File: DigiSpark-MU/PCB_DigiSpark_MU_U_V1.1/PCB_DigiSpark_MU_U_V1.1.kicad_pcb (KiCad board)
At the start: 2 copper layers, 17 x 12 mm, 14 parts, among them J1 USB_A, J2 Conn_01x04, SW1 SW_Push

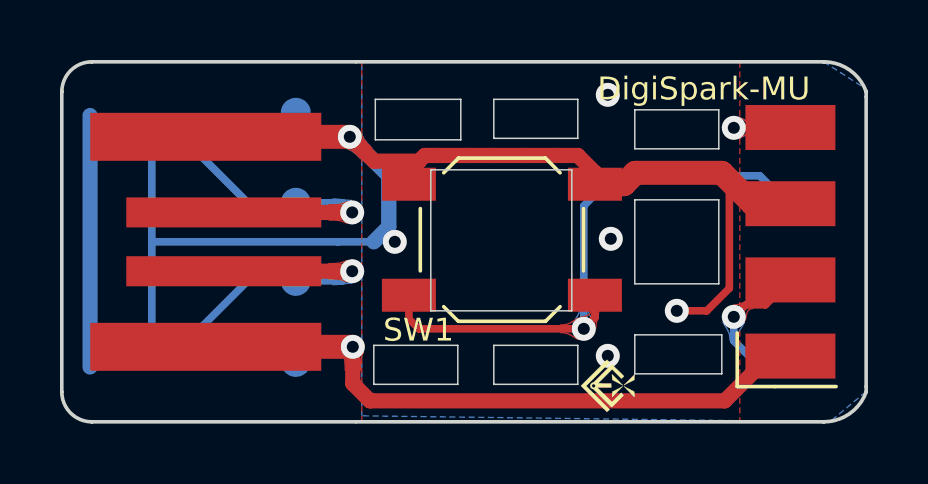
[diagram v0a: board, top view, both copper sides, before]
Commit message: fix silks
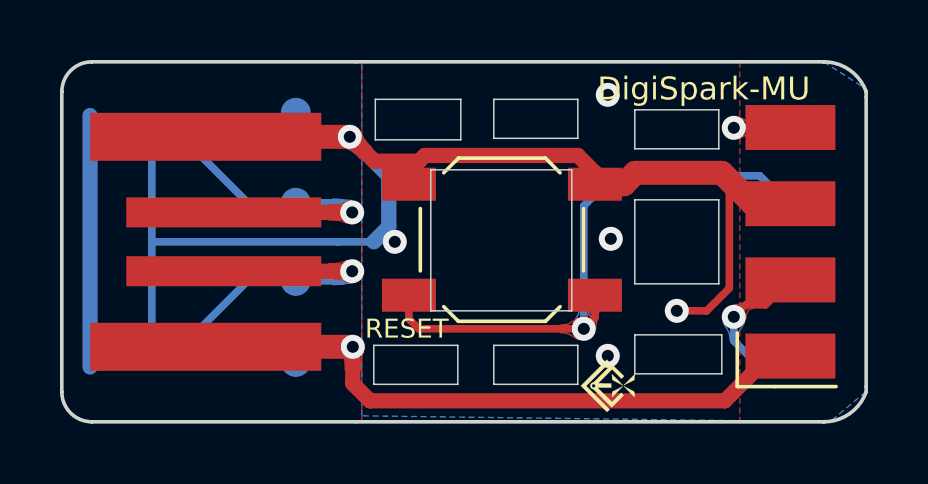
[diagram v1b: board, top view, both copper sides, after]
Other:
- board text added: "RESET"
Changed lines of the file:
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@@
   (general
     (thickness 1)
-    (drawings 40)
+    (drawings 41)
     (tracks 88)
     (zones 0)
@@
   (title_block
     (title PCB_DigiSpark_MU_U)
+    (rev V1.2)
     (company LEXSION.COM)
   )
@@
     (tags "SPST Button Switch")
     (attr smd)
-    (fp_text reference SW1 (at 2.7813 -3.0099) (layer F.SilkS)
+    (fp_text reference SW1 (at 2.7813 -3.0099) (layer F.SilkS) hide
       (effects (font (size 0.762 0.762) (thickness 0.127)))
     )
@@
     (tags "test point SMD pad")
     (attr virtual)
-    (fp_text reference TP6 (at 0.3894 1.107866) (layer B.SilkS)
+    (fp_text reference TP6 (at 0.3 1.333334) (layer B.SilkS)
       (effects (font (size 1 1) (thickness 0.15)) (justify mirror))
     )
@@
     (tags "test point SMD pad")
     (attr virtual)
-    (fp_text reference TP5 (at 0.364 1.114533) (layer B.SilkS)
+    (fp_text reference TP5 (at 0.3 1.366667) (layer B.SilkS)
       (effects (font (size 1 1) (thickness 0.15)) (justify mirror))
     )
@@
     (tags "test point SMD pad")
     (attr virtual)
-    (fp_text reference TP4 (at 0.364 1.1466) (layer B.SilkS)
+    (fp_text reference TP4 (at 0.4 1.3) (layer B.SilkS)
       (effects (font (size 1 1) (thickness 0.15)) (justify mirror))
     )
@@
     (tags "test point SMD pad")
     (attr virtual)
-    (fp_text reference TP3 (at 0.3132 1.0758) (layer B.SilkS)
+    (fp_text reference TP3 (at 0.3 1.3) (layer B.SilkS)
       (effects (font (size 1.016 1) (thickness 0.1524)) (justify mirror))
     )
@@
     (tags "test point SMD pad")
     (attr virtual)
-    (fp_text reference TP2 (at -2.032 0.3418) (layer B.SilkS)
+    (fp_text reference TP2 (at -1.9 -0.6) (layer B.SilkS)
       (effects (font (size 1 1) (thickness 0.15)) (justify mirror))
     )
@@
     (tags "test point SMD pad")
     (attr virtual)
-    (fp_text reference TP1 (at -2.032 -0.6292) (layer B.SilkS)
+    (fp_text reference TP1 (at -2.2 0.8) (layer B.SilkS)
       (effects (font (size 1 1) (thickness 0.15)) (justify mirror))
     )
@@
     (tags "Diode SOD523")
     (attr smd)
-    (fp_text reference D2 (at 0 1.3) (layer B.SilkS)
+    (fp_text reference D2 (at 0.8 1.3) (layer B.SilkS)
       (effects (font (size 1 1) (thickness 0.15)) (justify mirror))
     )
@@
     (tags "Diode SOD523")
     (attr smd)
-    (fp_text reference D1 (at 0 1.3) (layer B.SilkS)
+    (fp_text reference D1 (at 1 1.3) (layer B.SilkS)
       (effects (font (size 1 1) (thickness 0.15)) (justify mirror))
     )
@@
     )
   )
+  (gr_text RESET (at 118 41.4) (layer F.SilkS)
+    (effects (font (size 0.635 0.635) (thickness 0.1016)))
+  )
   (gr_text DigiSpark-MU (at 127.9 33.4) (layer F.SilkS)
